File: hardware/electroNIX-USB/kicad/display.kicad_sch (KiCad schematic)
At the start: 69 parts, among them Q10 MMBTA42, Q11 MMBTA92, Q12 MMBTA42, Q13 MMBTA42, Q14 MMBTA42, Q15 MMBTA42, Q16 MMBTA42, Q17 MMBTA42, Q18 MMBTA42, Q19 MMBTA42, Q20 MMBTA42, Q21 MMBTA42, Q22 MMBTA42, Q23 MMBTA42, Q4 MMBTA42, Q5 MMBTA92, Q6 MMBTA42, Q7 MMBTA92, Q8 MMBTA42, Q9 MMBTA92

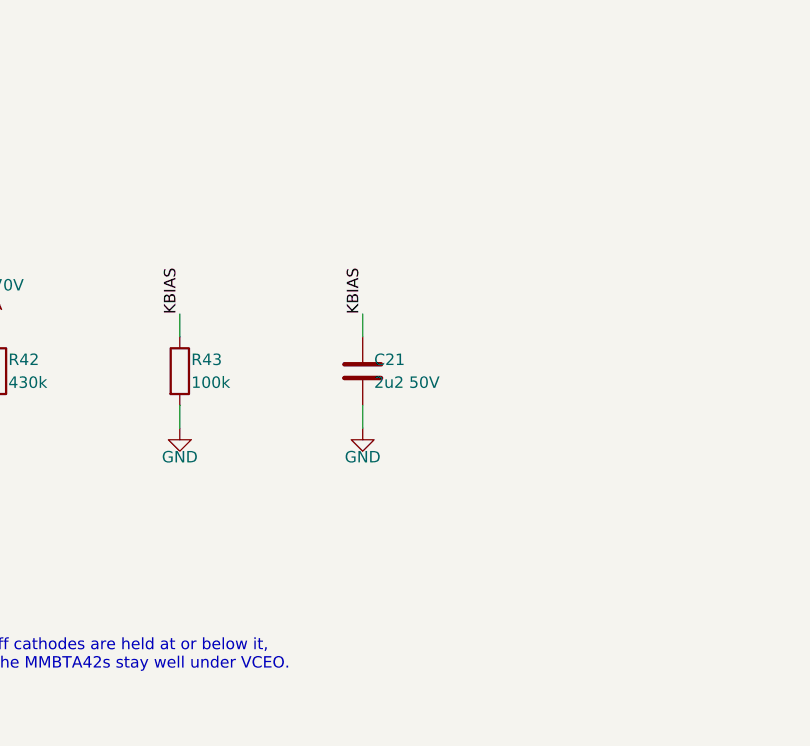
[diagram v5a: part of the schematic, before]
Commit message: electroNIX-USB: restore PCB-036 KBIAS capacitor string (4 x 470n in series)
C41-C44 on PCB-036 are in series (118 nF, 200 V string) across R46, not
in parallel. Replace the single 2.2 uF/50 V cap with the original series
string and place it beside the 430k/100k divider.

Co-Authored-By: Claude Opus 5.5 <noreply@anthropic.com>
Claude-Session: https://claude.ai/code/session_01AFMfevKEKDGbci8uJGhf4W
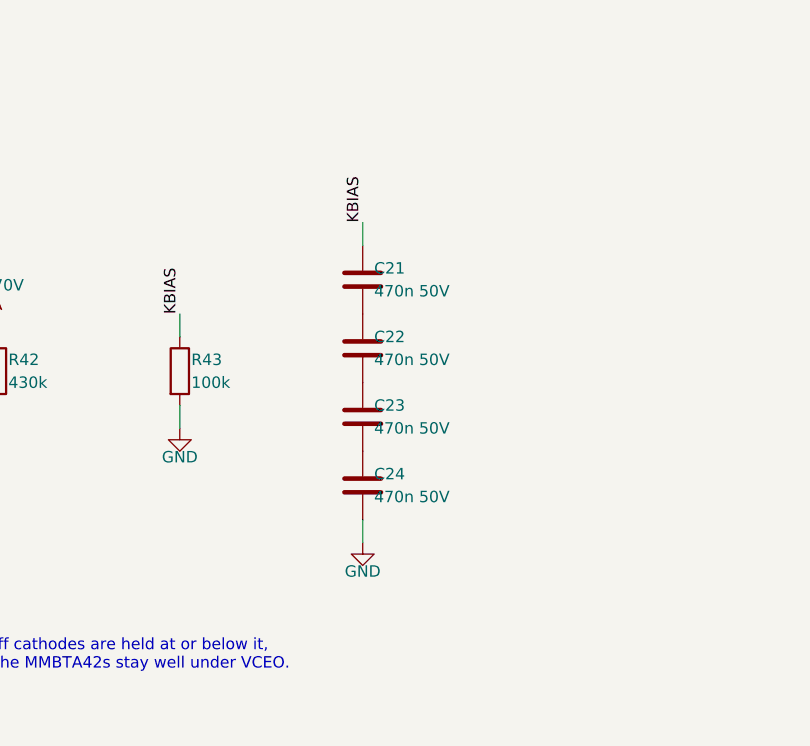
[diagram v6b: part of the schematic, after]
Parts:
- added C22, C23, C24: 470n 50V, Capacitor_SMD:C_0805_2012Metric, symbol Device:C
- C21: value 2u2 50V -> 470n 50V; footprint Capacitor_SMD:C_1206_3216Metric -> Capacitor_SMD:C_0805_2012Metric
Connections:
- net GND: now also C24.2; no longer C21.2
- new net: C21.2, C22.1
- new net: C22.2, C23.1
- new net: C23.2, C24.1
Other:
- moved on the sheet: C21
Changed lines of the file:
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@@
   (wire
     (pts
-      (xy 490.22 246.38)
-      (xy 490.22 243.84))
+      (xy 490.22 236.22)
+      (xy 490.22 233.68))
     (stroke
       (width 0)
@@
   (wire
     (pts
-      (xy 490.22 254)
-      (xy 490.22 256.54))
+      (xy 490.22 266.7)
+      (xy 490.22 269.24))
     (stroke
       (width 0)
@@
 )
   (label "KBIAS"
-    (at 490.22 243.84 90)
+    (at 490.22 233.68 90)
     (fields_autoplaced)
     (effects
@@
           (unit 1)))))
   (symbol
+    (lib_id "Device:C")
+    (at 490.22 240.03 0)
+    (unit 1)
+    (in_bom yes)
+    (on_board yes)
+    (dnp no)
+    (property "Reference" "C21"
+      (at 491.49 238.76 0)
+      (effects
+        (font
+          (size 1.27 1.27))
+        (justify left)))
+    (property "Value" "470n 50V"
+      (at 491.49 241.3 0)
+      (effects
+        (font
+          (size 1.27 1.27))
+        (justify left)))
+    (property "Footprint" "Capacitor_SMD:C_0805_2012Metric"
+      (at 490.22 240.03 0)
+      (effects
+        (font
+          (size 1.27 1.27))
+        (justify left) hide))
+    (property "Datasheet" "~"
+      (at 490.22 240.03 0)
+      (effects
+        (font
+          (size 1.27 1.27))
+        (justify left) hide))
+    (pin "1"
+)
+    (pin "2"
+)
+    (instances
+      (project "electroNIX-USB"
+        (path "/af167dc7-e2c9-570c-bdf4-28156a519677/e1c1bd65-1db2-544e-8cf9-3d73564eba6a"
+          (reference "C21")
+          (unit 1)))))
+  (symbol
+    (lib_id "Device:C")
+    (at 490.22 247.65 0)
+    (unit 1)
+    (in_bom yes)
+    (on_board yes)
+    (dnp no)
+    (property "Reference" "C22"
+      (at 491.49 246.38 0)
+      (effects
+        (font
+          (size 1.27 1.27))
+        (justify left)))
+    (property "Value" "470n 50V"
+      (at 491.49 248.92 0)
+      (effects
+        (font
+          (size 1.27 1.27))
+        (justify left)))
+    (property "Footprint" "Capacitor_SMD:C_0805_2012Metric"
+      (at 490.22 247.65 0)
+      (effects
+        (font
+          (size 1.27 1.27))
+        (justify left) hide))
+    (property "Datasheet" "~"
+      (at 490.22 247.65 0)
+      (effects
+        (font
+          (size 1.27 1.27))
+        (justify left) hide))
+    (pin "1"
+)
+    (pin "2"
+)
+    (instances
+      (project "electroNIX-USB"
+        (path "/af167dc7-e2c9-570c-bdf4-28156a519677/e1c1bd65-1db2-544e-8cf9-3d73564eba6a"
+          (reference "C22")
+          (unit 1)))))
+  (symbol
+    (lib_id "Device:C")
+    (at 490.22 255.27 0)
+    (unit 1)
+    (in_bom yes)
+    (on_board yes)
+    (dnp no)
+    (property "Reference" "C23"
+      (at 491.49 254 0)
+      (effects
+        (font
+          (size 1.27 1.27))
+        (justify left)))
+    (property "Value" "470n 50V"
+      (at 491.49 256.54 0)
+      (effects
+        (font
+          (size 1.27 1.27))
+        (justify left)))
+    (property "Footprint" "Capacitor_SMD:C_0805_2012Metric"
+      (at 490.22 255.27 0)
+      (effects
+        (font
+          (size 1.27 1.27))
+        (justify left) hide))
+    (property "Datasheet" "~"
+      (at 490.22 255.27 0)
+      (effects
+        (font
+          (size 1.27 1.27))
+        (justify left) hide))
+    (pin "1"
+)
+    (pin "2"
+)
+    (instances
+      (project "electroNIX-USB"
+        (path "/af167dc7-e2c9-570c-bdf4-28156a519677/e1c1bd65-1db2-544e-8cf9-3d73564eba6a"
+          (reference "C23")
+          (unit 1)))))
+  (symbol
     (lib_id "power:GND")
-    (at 490.22 256.54 0)
+    (at 490.22 269.24 0)
     (unit 1)
     (in_bom yes)
     (on_board yes)
     (dnp no)
-    (property "Reference" "#PWR5096"
-      (at 490.22 256.54 0)
+    (property "Reference" "#PWR5099"
+      (at 490.22 269.24 0)
       (effects
         (font
           (size 1.27 1.27)) hide))
     (property "Value" "GND"
-      (at 490.22 259.74 0)
+      (at 490.22 272.44 0)
       (effects
         (font
           (size 1.27 1.27))))
     (property "Footprint" ""
-      (at 490.22 256.54 0)
+      (at 490.22 269.24 0)
       (effects
         (font
           (size 1.27 1.27)) hide))
     (property "Datasheet" ""
-      (at 490.22 256.54 0)
+      (at 490.22 269.24 0)
       (effects
         (font
@@
       (project "electroNIX-USB"
         (path "/af167dc7-e2c9-570c-bdf4-28156a519677/e1c1bd65-1db2-544e-8cf9-3d73564eba6a"
-          (reference "#PWR5096")
+          (reference "#PWR5099")
           (unit 1)))))
   (symbol
     (lib_id "Device:C")
-    (at 490.22 250.19 0)
+    (at 490.22 262.89 0)
     (unit 1)
     (in_bom yes)
     (on_board yes)
     (dnp no)
-    (property "Reference" "C21"
-      (at 491.49 248.92 0)
+    (property "Reference" "C24"
+      (at 491.49 261.62 0)
       (effects
         (font
           (size 1.27 1.27))
         (justify left)))
-    (property "Value" "2u2 50V"
-      (at 491.49 251.46 0)
+    (property "Value" "470n 50V"
+      (at 491.49 264.16 0)
       (effects
         (font
           (size 1.27 1.27))
         (justify left)))
-    (property "Footprint" "Capacitor_SMD:C_1206_3216Metric"
-      (at 490.22 250.19 0)
+    (property "Footprint" "Capacitor_SMD:C_0805_2012Metric"
+      (at 490.22 262.89 0)
       (effects
         (font
@@
         (justify left) hide))
     (property "Datasheet" "~"
-      (at 490.22 250.19 0)
+      (at 490.22 262.89 0)
       (effects
         (font
@@
       (project "electroNIX-USB"
         (path "/af167dc7-e2c9-570c-bdf4-28156a519677/e1c1bd65-1db2-544e-8cf9-3d73564eba6a"
-          (reference "C21")
+          (reference "C24")
           (unit 1))))))
